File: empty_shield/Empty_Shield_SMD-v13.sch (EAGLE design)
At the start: 18 parts

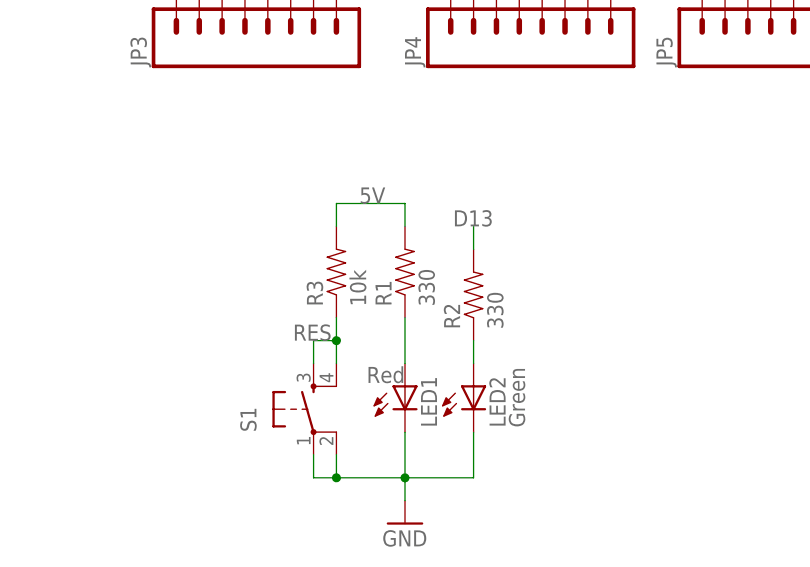
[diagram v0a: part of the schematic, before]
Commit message: empty shield SMD
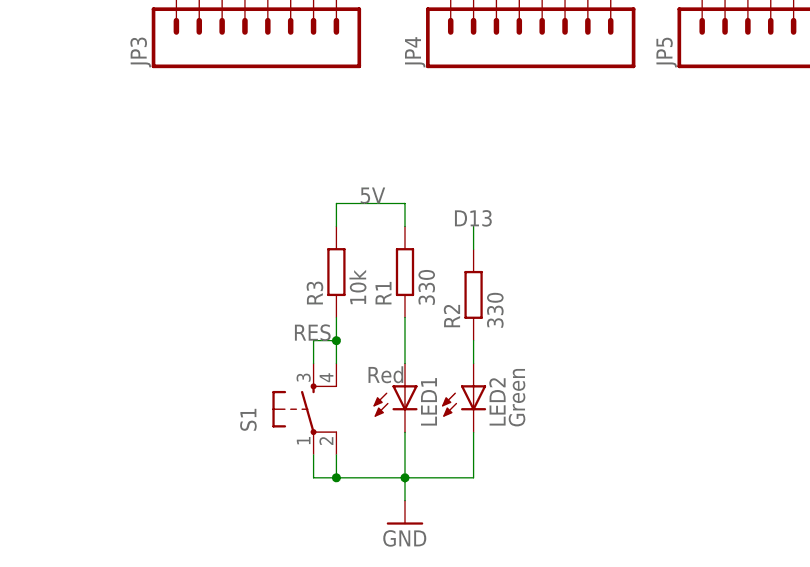
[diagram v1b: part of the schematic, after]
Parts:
- LED1, LED2: device SparkFun:LED5MM -> led:LEDCHIP-LED0805
- R1, R2, R3: device SparkFun:RESISTORPTH1 -> rcl:R-EU_R0805
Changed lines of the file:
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@@
 <part name="JP12" library="SparkFun" deviceset="M02" device="LOCK"/>
 <part name="S1" library="SparkFun" deviceset="TAC_SWITCH" device="PTH"/>
-<part name="LED1" library="SparkFun" deviceset="LED" device="5MM" value="Red"/>
-<part name="LED2" library="SparkFun" deviceset="LED" device="5MM" value="Green"/>
-<part name="R1" library="SparkFun" deviceset="RESISTOR" device="PTH1" value="330"/>
-<part name="R2" library="SparkFun" deviceset="RESISTOR" device="PTH1" value="330"/>
-<part name="R3" library="SparkFun" deviceset="RESISTOR" device="PTH1" value="10k"/>
+<part name="LED1" library="led" deviceset="LED" device="CHIP-LED0805" value="Red"/>
+<part name="LED2" library="led" deviceset="LED" device="CHIP-LED0805" value="Green"/>
+<part name="R1" library="rcl" deviceset="R-EU_" device="R0805" value="330"/>
+<part name="R2" library="rcl" deviceset="R-EU_" device="R0805" value="330"/>
+<part name="R3" library="rcl" deviceset="R-EU_" device="R0805" value="10k"/>
 <part name="GND1" library="SparkFun" deviceset="GND" device=""/>
 <part name="GND2" library="SparkFun" deviceset="GND" device=""/>
